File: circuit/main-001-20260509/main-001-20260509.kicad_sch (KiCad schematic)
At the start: 13 parts, among them Q1 BSS138, Q2 BSS138, U1 DEV-16771

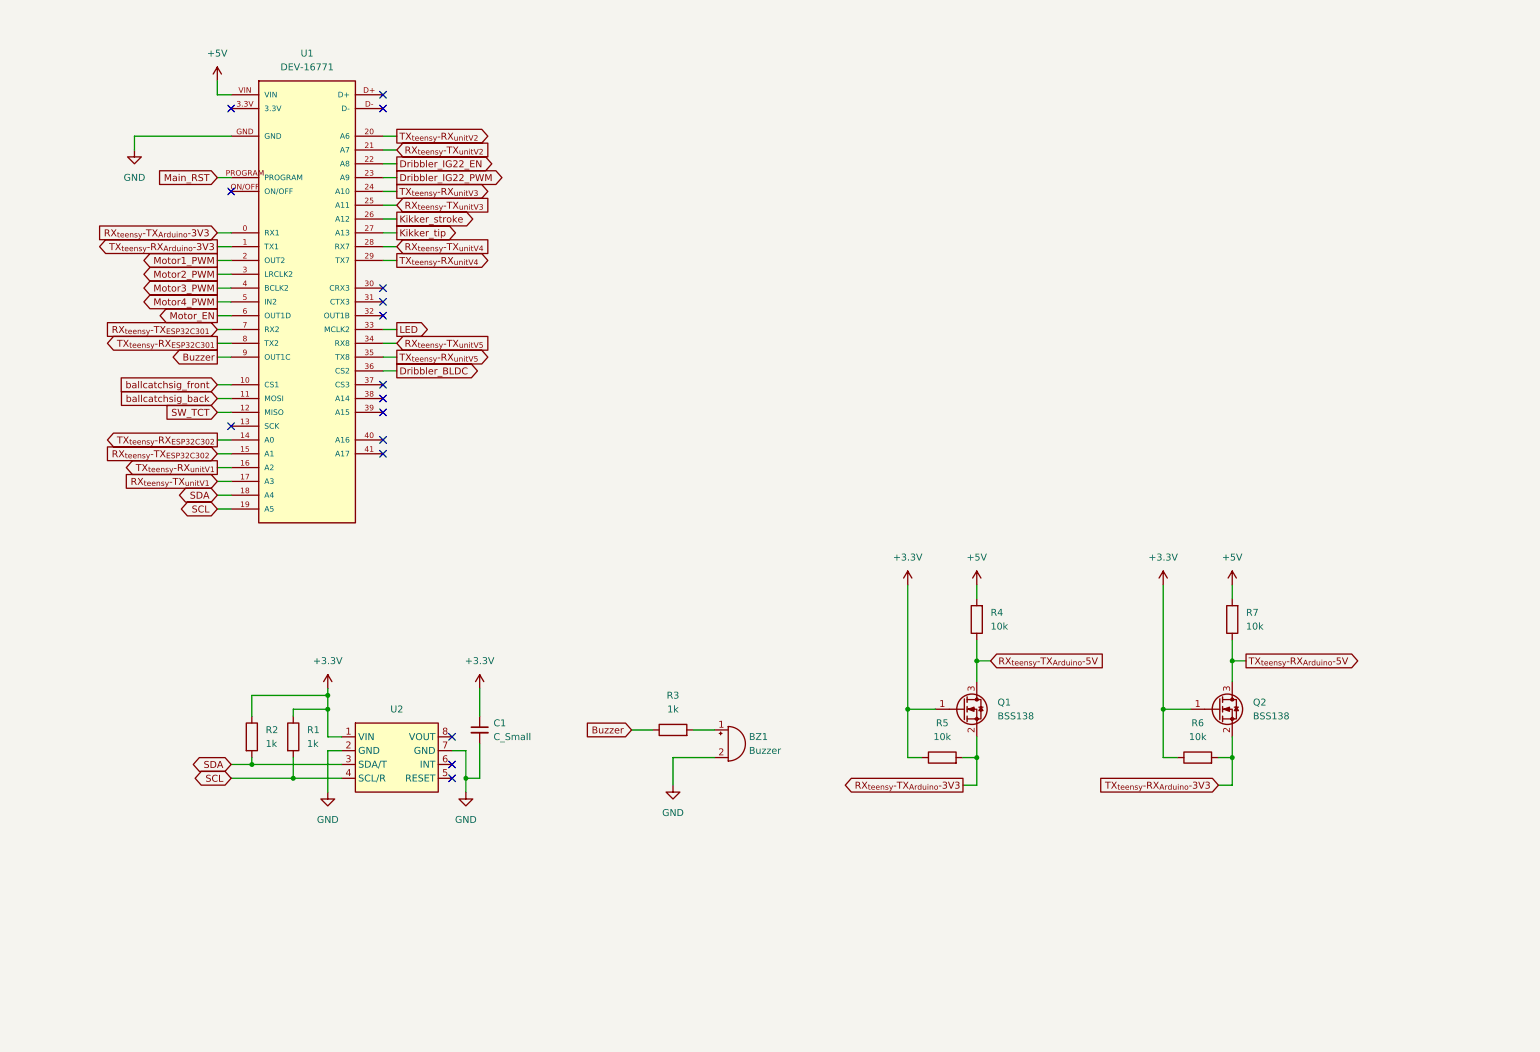
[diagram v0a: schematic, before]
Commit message: Update メイン基板の回路図をリファクタリングした
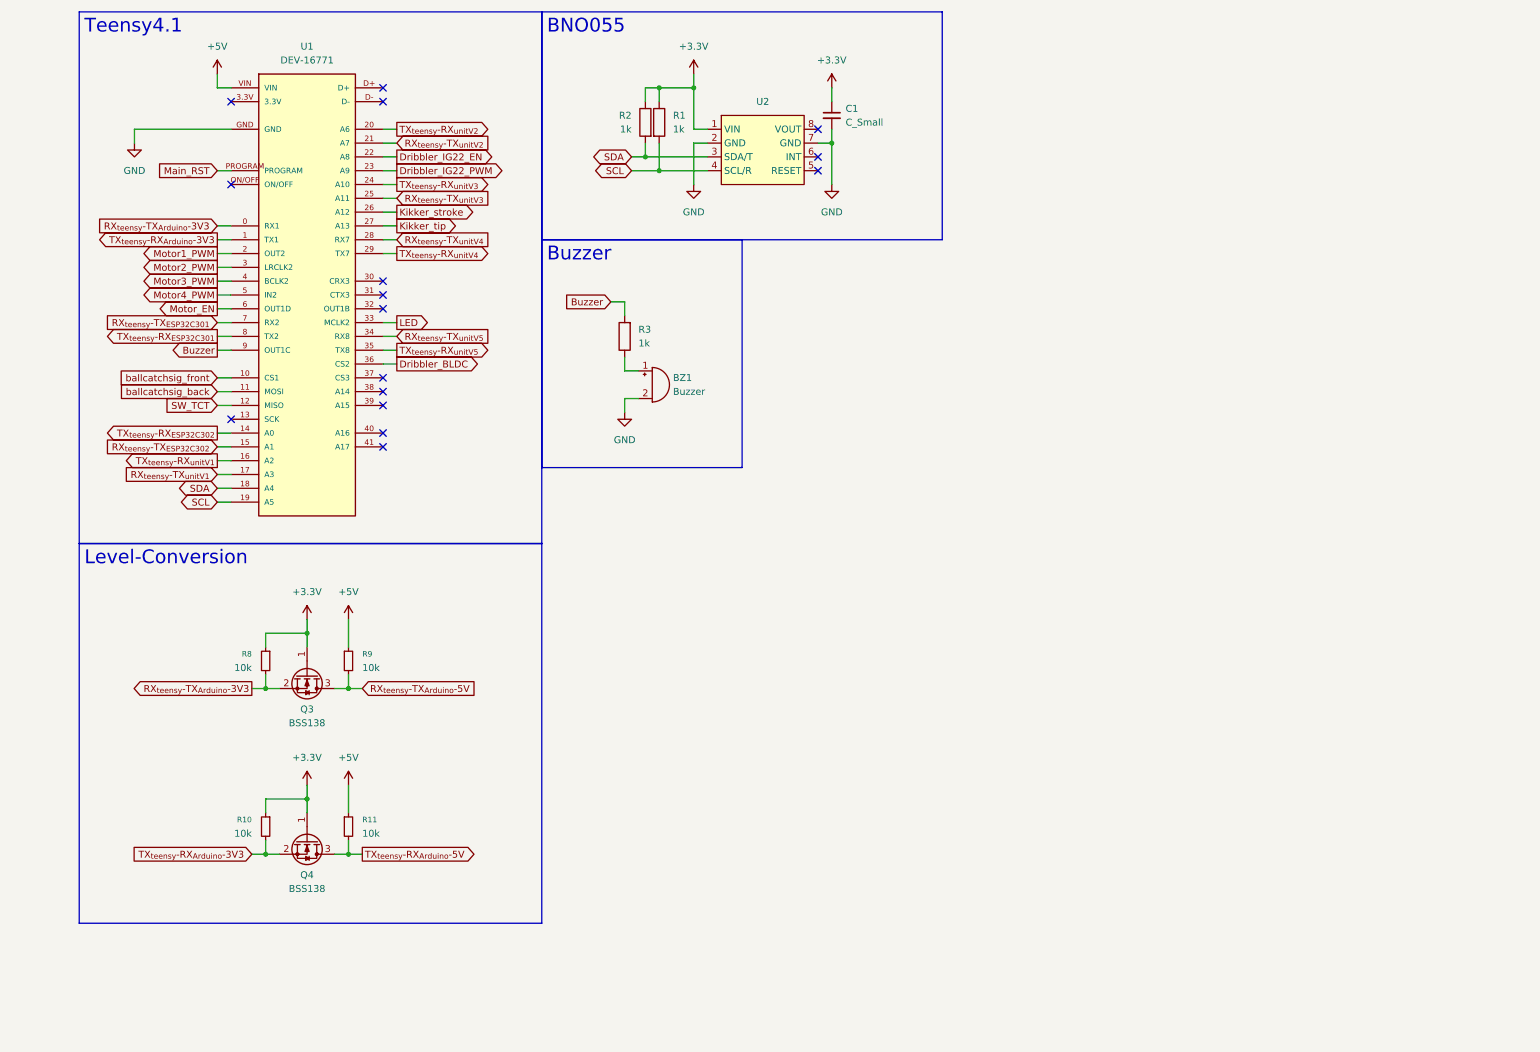
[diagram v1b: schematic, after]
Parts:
- removed Q1, Q2: BSS138, Package_TO_SOT_SMD:SOT-23, symbol Transistor_FET:BSS138
- removed R4, R5, R6, R7: 10k, symbol Device:R
- added Q3, Q4: BSS138, Package_TO_SOT_SMD:SOT-23, symbol Transistor_FET:BSS138
- added R10, R11, R8, R9: 10k, symbol Device:R_Small
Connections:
- net +3.3V: now also Q3.1 (G), Q4.1 (G), R10.1, R8.1
- net +5V: now also R11.1, R9.1
- net Buzzer: now also R3.2; no longer R3.1
- net RX_{teensy}-TX_{Arduino}-3V3: now also Q3.2 (S), R8.2
- net RX_{teensy}-TX_{Arduino}-5V: now also Q3.3 (D), R9.2
- net TX_{teensy}-RX_{Arduino}-3V3: now also Q4.2 (S), R10.2
- net TX_{teensy}-RX_{Arduino}-5V: now also Q4.3 (D), R11.2
- net at BZ1.1 (+): now also R3.1; no longer R3.2
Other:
- moved on the sheet: BZ1, C1, R1, R2, R3, U1, U2

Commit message: Update メイン基板の回路図仮完成
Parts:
- added C2: 100n, Capacitor_SMD:C_0805_2012Metric, symbol Device:C_Small
- added D1: LED_Small, symbol Device:LED_Small
- added J1: Conn_Relay, Connector_PinSocket_2.54mm:PinSocket_2x08_P2.54mm_Vertical, symbol Connector_Generic:Conn_02x08_Counter_Clockwise
- added J2: Conn_Sub, symbol Connector:Conn_01x18_Pin
- added R8: 10k, Resistor_SMD:R_0805_2012Metric, symbol Device:R_Small
- added R9: 330, Resistor_SMD:R_0805_2012Metric, symbol Device:R_Small
- added SW1: RESET, symbol Switch:SW_SPST
- C1: value C_Small -> 100n; footprint (none) -> Capacitor_SMD:C_0805_2012Metric
- R1: renamed from R8; footprint (none) -> Resistor_SMD:R_0805_2012Metric
- R2: renamed from R10; footprint (none) -> Resistor_SMD:R_0805_2012Metric
- R3: renamed from R9; footprint (none) -> Resistor_SMD:R_0805_2012Metric
- R4: renamed from R11; footprint (none) -> Resistor_SMD:R_0805_2012Metric
- R5: renamed from R2; footprint (none) -> Resistor_SMD:R_0805_2012Metric
- R6: renamed from R3; footprint (none) -> Resistor_SMD:R_0805_2012Metric
- R7: renamed from R1; footprint (none) -> Resistor_SMD:R_0805_2012Metric
- U1: footprint @2024TOINIOT2-Main:MODULE_DEV-16771 -> @Thrive_footprint_main:DEV-16771
- U2: value (none) -> BNO055; footprint (none) -> @Thrive_footprint_main:BNO055
- renumbered Q3 to Q1, Q4 to Q2
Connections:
- net +3.3V: now also U2.7 (GND), J1.1 (Pin_1), J2.1 (Pin_1), R8.1
- net GND: now also C2.2, D1.1 (K), J2.2 (Pin_2), J2.3 (Pin_3), SW1.2 (B); no longer U2.7 (GND)
- net LED: now also R9.1
- net Main_RST: now also C2.1, R8.2, SW1.1 (A)
- net RX_{teensy}-TX_{Arduino}-5V: now also J1.7 (Pin_7)
- net RX_{teensy}-TX_{ESP32C301}: now also J2.16 (Pin_16)
- net RX_{teensy}-TX_{ESP32C302}: now also J2.18 (Pin_18)
- net RX_{teensy}-TX_{unitV1}: now also J2.6 (Pin_6)
- net RX_{teensy}-TX_{unitV2}: now also J2.8 (Pin_8)
- net RX_{teensy}-TX_{unitV3}: now also J2.10 (Pin_10)
- net RX_{teensy}-TX_{unitV4}: now also J2.12 (Pin_12)
- net RX_{teensy}-TX_{unitV5}: now also J2.14 (Pin_14)
- net TX_{teensy}-RX_{Arduino}-5V: now also J1.8 (Pin_8)
- net TX_{teensy}-RX_{ESP32C301}: now also J2.15 (Pin_15)
- net TX_{teensy}-RX_{ESP32C302}: now also J2.17 (Pin_17)
- net TX_{teensy}-RX_{unitV1}: now also J2.5 (Pin_5)
- net TX_{teensy}-RX_{unitV2}: now also J2.7 (Pin_7)
- net TX_{teensy}-RX_{unitV3}: now also J2.9 (Pin_9)
- net TX_{teensy}-RX_{unitV4}: now also J2.11 (Pin_11)
- net TX_{teensy}-RX_{unitV5}: now also J2.13 (Pin_13)
- net EN_{BOOST}: now reaches U1.30 (CRX3)
- net EN_{BOOST}: now also U1.37 (CS3), J1.14 (Pin_14)
- net Dribbler_BLDC renamed Dribbler_{Back}
- net Dribbler_{Back}: now also J1.9 (Pin_9)
- net Dribbler_IG22_EN renamed Dribbler_{Front-EN}
- net Dribbler_{Front-EN}: now also J1.11 (Pin_11)
- net Dribbler_IG22_PWM renamed Dribbler_{Front-PWM}
- net Dribbler_{Front-PWM}: now also J1.10 (Pin_10)
- net Kikker_stroke renamed Kicker_{Stroke}
- net Kicker_{Stroke}: now also J1.16 (Pin_16)
- net Kikker_tip renamed Kicker_{Tip}
- net Kicker_{Tip}: now also J1.15 (Pin_15)
- net Motor1_PWM renamed Motor1_{PWM}
- net Motor1_{PWM}: now also J1.2 (Pin_2)
- net Motor2_PWM renamed Motor2_{PWM}
- net Motor2_{PWM}: now also J1.3 (Pin_3)
- net Motor3_PWM renamed Motor3_{PWM}
- net Motor3_{PWM}: now also J1.4 (Pin_4)
- net Motor4_PWM renamed Motor4_{PWM}
- net Motor4_{PWM}: now also J1.5 (Pin_5)
- net Motor_EN renamed Motor_{EN}
- net Motor_{EN}: now also J1.6 (Pin_6)
- net SW_TCT renamed SW_{START}
- net SW_{START}: now also J2.4 (Pin_4)
- net ballcatchsig_back renamed BallCatch_{Back}
- net BallCatch_{Back}: now also J1.12 (Pin_12)
- net ballcatchsig_front renamed BallCatch_{Front}
- net BallCatch_{Front}: now also J1.13 (Pin_13)
- new net: D1.2 (A), R9.2
- no-connect marks 16 -> 14
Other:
- moved on the sheet: BZ1, C1, R5, R6, R7

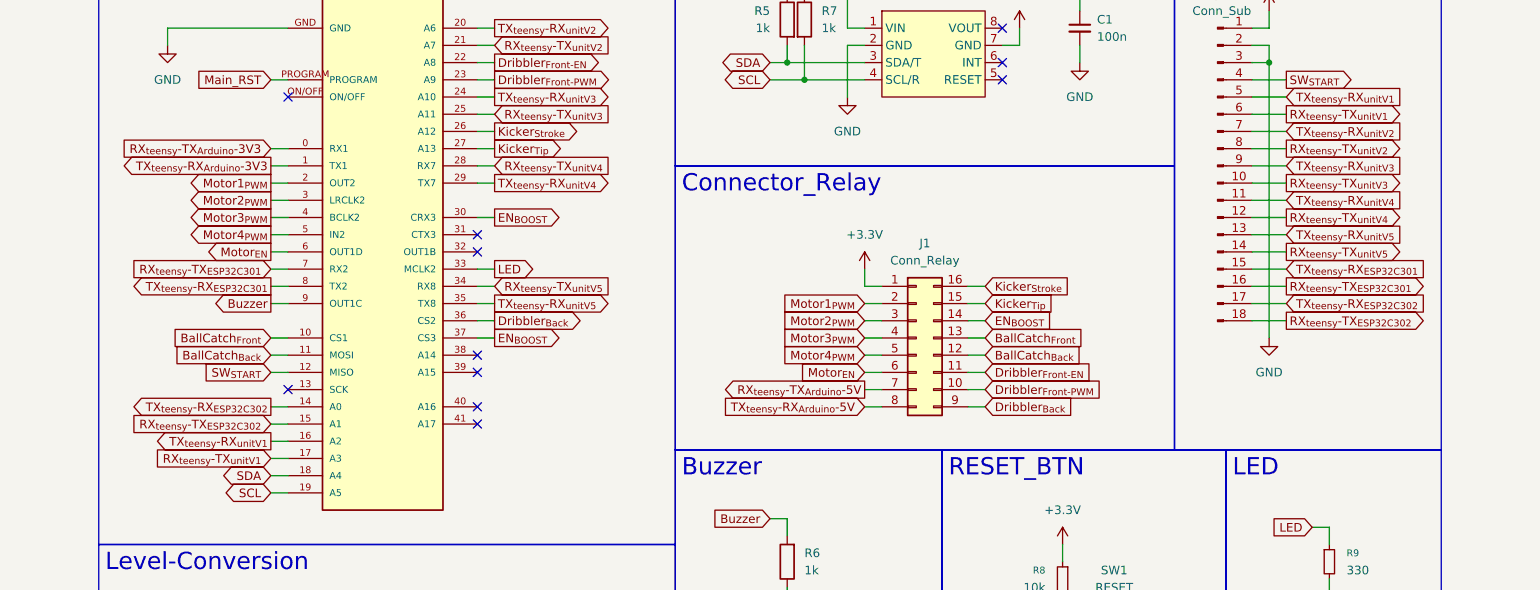
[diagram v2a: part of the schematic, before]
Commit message: Update メイン基板のボード図に入った
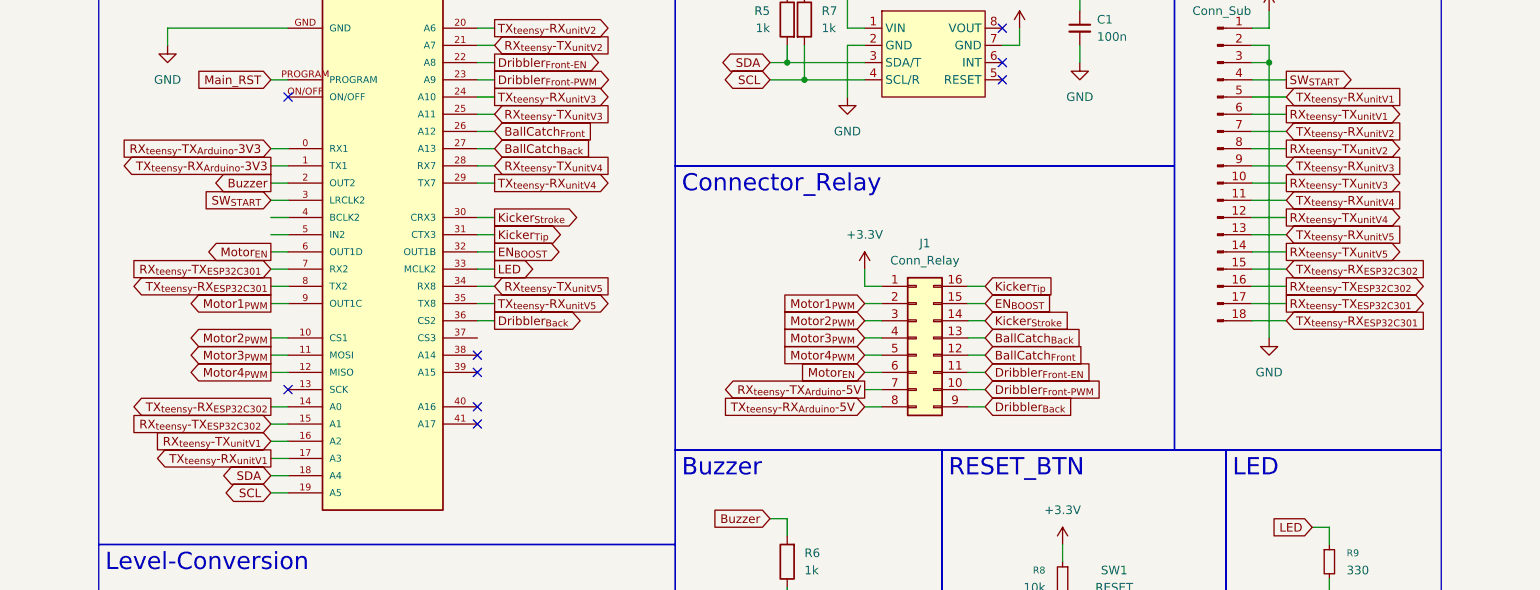
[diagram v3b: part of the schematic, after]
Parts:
- BZ1: footprint (none) -> @Thrive_footprint_main:PKM13EPYH4000-A0
- D1: footprint (none) -> LED_SMD:LED_0603_1608Metric
- J2: footprint (none) -> @Thrive_footprint_main:FPC-05F-18PH20
- SW1: footprint (none) -> @Thrive_footprint_main:TVBP06-B043C
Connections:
- net BallCatch_{Back}: now also J1.13 (Pin_13), U1.27 (A13); no longer J1.12 (Pin_12), U1.11 (MOSI)
- net BallCatch_{Front}: now also J1.12 (Pin_12), U1.26 (A12); no longer J1.13 (Pin_13), U1.10 (CS1)
- net Buzzer: now also U1.2 (OUT2); no longer U1.9 (OUT1C)
- net EN_{BOOST}: now also J1.15 (Pin_15), U1.32 (OUT1B); no longer J1.14 (Pin_14), U1.30 (CRX3), U1.37 (CS3)
- net Kicker_{Stroke}: now also J1.14 (Pin_14), U1.30 (CRX3); no longer J1.16 (Pin_16), U1.26 (A12)
- net Kicker_{Tip}: now also J1.16 (Pin_16), U1.31 (CTX3); no longer J1.15 (Pin_15), U1.27 (A13)
- net Motor1_{PWM}: now also U1.9 (OUT1C); no longer U1.2 (OUT2)
- net Motor2_{PWM}: now also U1.10 (CS1); no longer U1.3 (LRCLK2)
- net Motor3_{PWM}: now also U1.11 (MOSI); no longer U1.4 (BCLK2)
- net Motor4_{PWM}: now also U1.12 (MISO); no longer U1.5 (IN2)
- net RX_{teensy}-TX_{ESP32C301}: now also J2.17 (Pin_17); no longer J2.16 (Pin_16)
- net RX_{teensy}-TX_{ESP32C302}: now also J2.16 (Pin_16); no longer J2.18 (Pin_18)
- net RX_{teensy}-TX_{unitV1}: now also U1.16 (A2); no longer U1.17 (A3)
- net SW_{START}: now also U1.3 (LRCLK2); no longer U1.12 (MISO)
- net TX_{teensy}-RX_{ESP32C301}: now also J2.18 (Pin_18); no longer J2.15 (Pin_15)
- net TX_{teensy}-RX_{ESP32C302}: now also J2.15 (Pin_15); no longer J2.17 (Pin_17)
- net TX_{teensy}-RX_{unitV1}: now also U1.17 (A3); no longer U1.16 (A2)
- no-connect marks 14 -> 12

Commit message: Update メイン基板のPCB完成
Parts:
- removed J1: Conn_Relay, Connector_PinSocket_2.54mm:PinSocket_2x08_P2.54mm_Vertical, symbol Connector_Generic:Conn_02x08_Counter_Clockwise
- added J1: Conn_02x09_Odd_Even, Connector_PinHeader_2.54mm:PinHeader_2x09_P2.54mm_Vertical, symbol Connector_Generic:Conn_02x09_Odd_Even
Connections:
- net +3.3V: now also J2.10 (Pin_10), J1.10 (Pin_10); no longer J2.1 (Pin_1)
- net +5V: now also J2.11 (Pin_11), J1.12 (Pin_12)
- net BallCatch_{Back}: now also J1.14 (Pin_14)
- net BallCatch_{Front}: now also J1.11 (Pin_11)
- net Dribbler_{Back}: now also J1.15 (Pin_15)
- net Dribbler_{Front-EN}: now also J1.8 (Pin_8)
- net Dribbler_{Front-PWM}: now also J1.6 (Pin_6)
- net EN_{BOOST}: now also J1.18 (Pin_18)
- net GND: now also J2.12 (Pin_12), J1.13 (Pin_13); no longer J2.2 (Pin_2), J2.3 (Pin_3)
- net Kicker_{Stroke}: now also J1.17 (Pin_17)
- net Kicker_{Tip}: now also J1.16 (Pin_16)
- net Motor1_{PWM}: now also J1.3 (Pin_3)
- net Motor2_{PWM}: now also J1.5 (Pin_5)
- net Motor3_{PWM}: now also J1.7 (Pin_7)
- net Motor4_{PWM}: now also J1.9 (Pin_9)
- net Motor_{EN}: now also J1.1 (Pin_1)
- net RX_{teensy}-TX_{Arduino}-5V: now also J1.4 (Pin_4)
- net RX_{teensy}-TX_{ESP32C301}: now also J2.13 (Pin_13); no longer J2.17 (Pin_17)
- net RX_{teensy}-TX_{ESP32C302}: now also J2.6 (Pin_6); no longer J2.16 (Pin_16)
- net RX_{teensy}-TX_{unitV1}: now also J2.5 (Pin_5); no longer J2.6 (Pin_6)
- net RX_{teensy}-TX_{unitV2}: now also J2.1 (Pin_1); no longer J2.8 (Pin_8)
- net RX_{teensy}-TX_{unitV3}: now also J2.15 (Pin_15); no longer J2.10 (Pin_10)
- net RX_{teensy}-TX_{unitV4}: now also J2.18 (Pin_18); no longer J2.12 (Pin_12)
- net RX_{teensy}-TX_{unitV5}: now also J2.9 (Pin_9); no longer J2.14 (Pin_14)
- net SW_{START}: now also J2.3 (Pin_3); no longer J2.4 (Pin_4)
- net TX_{teensy}-RX_{Arduino}-5V: now also J1.2 (Pin_2)
- net TX_{teensy}-RX_{ESP32C301}: now also J2.14 (Pin_14); no longer J2.18 (Pin_18)
- net TX_{teensy}-RX_{ESP32C302}: now also J2.7 (Pin_7); no longer J2.15 (Pin_15)
- net TX_{teensy}-RX_{unitV1}: now also J2.4 (Pin_4); no longer J2.5 (Pin_5)
- net TX_{teensy}-RX_{unitV2}: now also J2.2 (Pin_2); no longer J2.7 (Pin_7)
- net TX_{teensy}-RX_{unitV3}: now also J2.16 (Pin_16); no longer J2.9 (Pin_9)
- net TX_{teensy}-RX_{unitV4}: now also J2.17 (Pin_17); no longer J2.11 (Pin_11)
- net TX_{teensy}-RX_{unitV5}: now also J2.8 (Pin_8); no longer J2.13 (Pin_13)

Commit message: Update メイン基板をDRした
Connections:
- net RX_{teensy}-TX_{ESP32C302}: now also J2.5 (Pin_5); no longer J2.6 (Pin_6)
- net RX_{teensy}-TX_{unitV1}: now also J2.4 (Pin_4); no longer J2.5 (Pin_5)
- net RX_{teensy}-TX_{unitV2}: now also J2.2 (Pin_2); no longer J2.1 (Pin_1)
- net SW_{START}: now also J2.8 (Pin_8), U1.5 (IN2); no longer J2.3 (Pin_3), U1.3 (LRCLK2)
- net TX_{teensy}-RX_{ESP32C302}: now also J2.6 (Pin_6); no longer J2.7 (Pin_7)
- net TX_{teensy}-RX_{unitV1}: now also J2.3 (Pin_3); no longer J2.4 (Pin_4)
- net TX_{teensy}-RX_{unitV2}: now also J2.1 (Pin_1); no longer J2.2 (Pin_2)
- net TX_{teensy}-RX_{unitV5}: now also J2.7 (Pin_7); no longer J2.8 (Pin_8)
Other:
- moved on the sheet: J2

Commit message: Update メイン基板いろいろまとめた
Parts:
- J1: value Conn_02x09_Odd_Even -> Conn_Relay
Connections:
- no-connect marks 12 -> 14
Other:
- moved on the sheet: C1, J1, R5, R7, U2
